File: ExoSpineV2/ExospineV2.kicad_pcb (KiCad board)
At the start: 2 copper layers, 79.5 x 73.1 mm, 54 parts, among them J1 JST PH 2pin, J11 2.54mm 4 pin header, J12 2.54mm 3 pin header, J13 JST PH 3pin, J14 JST PH 3pin, J15 JST PH 3pin, J16 JST PH 3pin, J17 JST PH 4pin, J18 JST PH 4pin, J19 2.54mm 4 pin header, J2 2.54mm 4 pin header, J20 2.54mm 3 pin header, J21 2.54mm 4 pin header, J22 2.54mm 3 pin header, J3 JST PH 3pin, J4 JST PH 3pin, J5 GPIO, J9 JST PH 2pin, Q4 2N7002, U1 MCP3008-I/SL, U2 74HC00, U3 74HC00

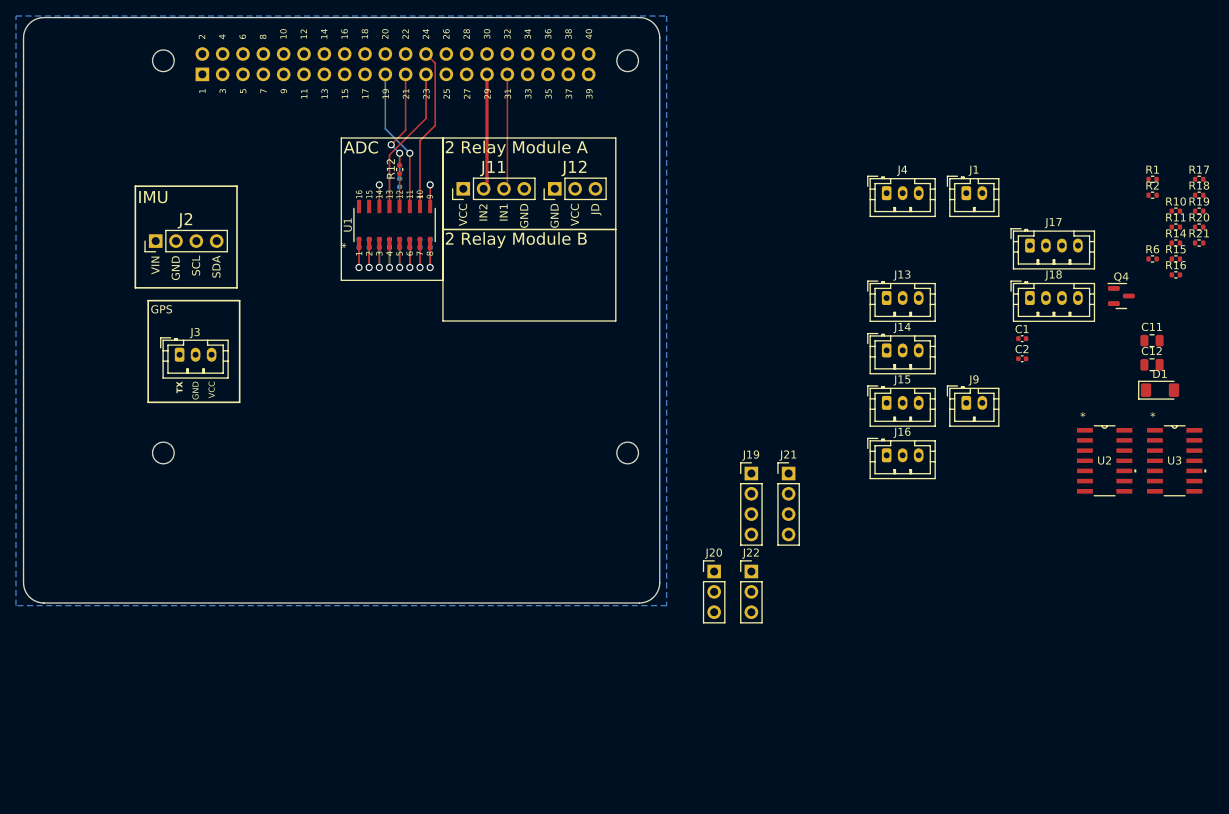
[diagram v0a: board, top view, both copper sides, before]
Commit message: positioned temperature sensors connectors on PCB
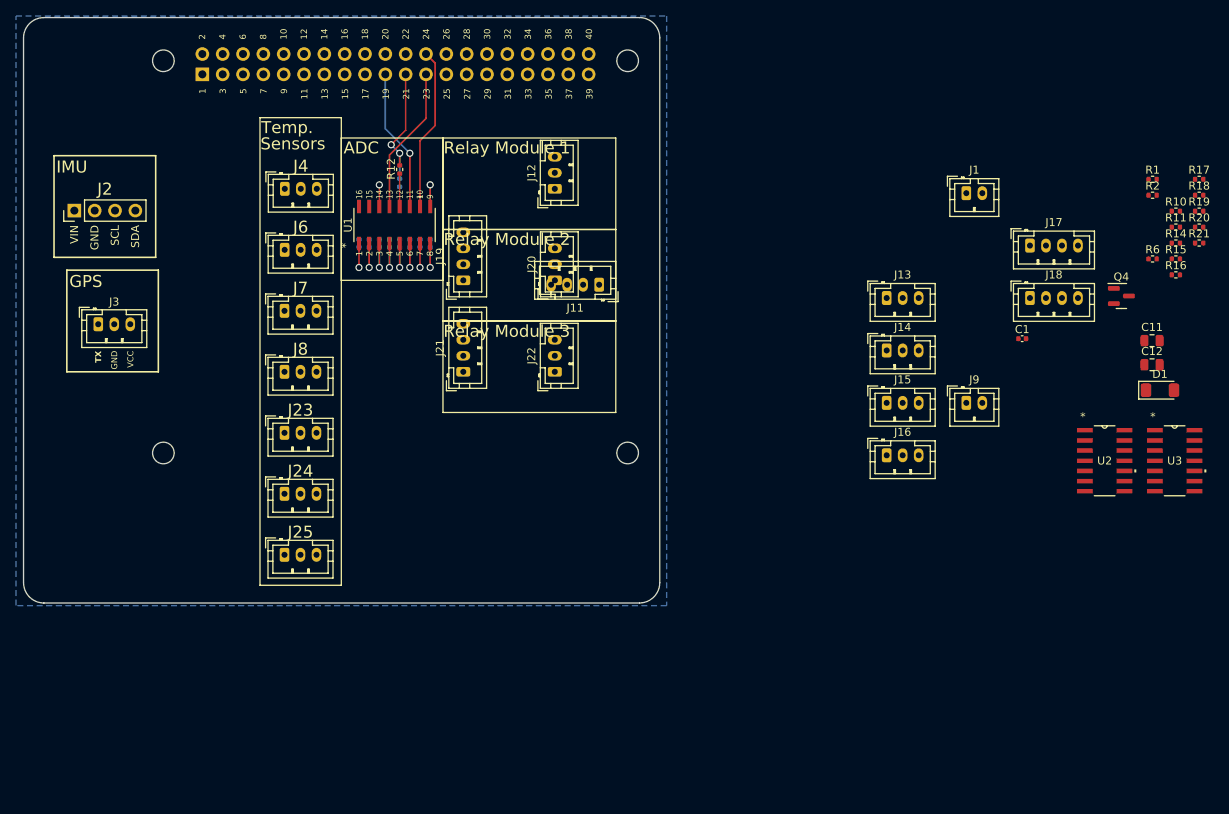
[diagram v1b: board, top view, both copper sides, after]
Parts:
- removed C2: 1uF, Capacitor_SMD:C_0402_1005Metric
- added J23: JST PH 3pin, Connector_JST:JST_PH_B3B-PH-K_1x03_P2.00mm_Vertical, F.Cu at (118.6, 94.0)
- added J24: JST PH 3pin, Connector_JST:JST_PH_B3B-PH-K_1x03_P2.00mm_Vertical, F.Cu at (118.6, 101.6)
- added J25: JST PH 3pin, Connector_JST:JST_PH_B3B-PH-K_1x03_P2.00mm_Vertical, F.Cu at (118.6, 109.2)
- added J6: JST PH 3pin, Connector_JST:JST_PH_B3B-PH-K_1x03_P2.00mm_Vertical, F.Cu at (118.7, 71.1)
- added J7: JST PH 3pin, Connector_JST:JST_PH_B3B-PH-K_1x03_P2.00mm_Vertical, F.Cu at (118.6, 78.7)
- added J8: JST PH 3pin, Connector_JST:JST_PH_B3B-PH-K_1x03_P2.00mm_Vertical, F.Cu at (118.6, 86.4)
- J11, J19, J21: value 2.54mm 4 pin header -> JST PH 4pin; footprint Connector_PinHeader_2.54mm:PinHeader_1x04_P2.54mm_Vertical -> Connector_JST:JST_PH_B4B-PH-K_1x04_P2.00mm_Vertical
- J12, J20, J22: value 2.54mm 3 pin header -> JST PH 3pin; footprint Connector_PinHeader_2.54mm:PinHeader_1x03_P2.54mm_Vertical -> Connector_JST:JST_PH_B3B-PH-K_1x03_P2.00mm_Vertical
- J2: value 2.54mm 4 pin header -> 2.54mm 4pin
- moved J4 75.2 mm to (118.7, 63.5)
- moved J19 43.3 mm to (141.0, 74.9), turned to 90 degrees
- moved J21 42.6 mm to (141.0, 86.4), turned to 90 degrees
- moved J20 41.5 mm to (152.4, 74.9), turned to 90 degrees
- moved J22 35.0 mm to (152.4, 86.4), turned to 90 degrees
- moved J11 20.8 mm to (157.9, 75.5), turned to 180 degrees
- moved J2 10.9 mm to (92.4, 66.2)
- moved J3 10.9 mm to (95.4, 80.4)
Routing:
- net /GPIO6: track 15.1 -> 0.00 mm
- net /GPIO5: track 15.1 -> 0.00 mm
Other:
- board text added: "Relay Module 1"
- board text added: "Relay Module 2"
- board text added: "Relay Module 3"
- board text added: "Sensors"
- board text added: "Temp."
- board text removed: "2 Relay Module A"
- board text removed: "2 Relay Module B"

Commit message: last commit before removing circuit for LTC4312 (I2C Multiplexer)
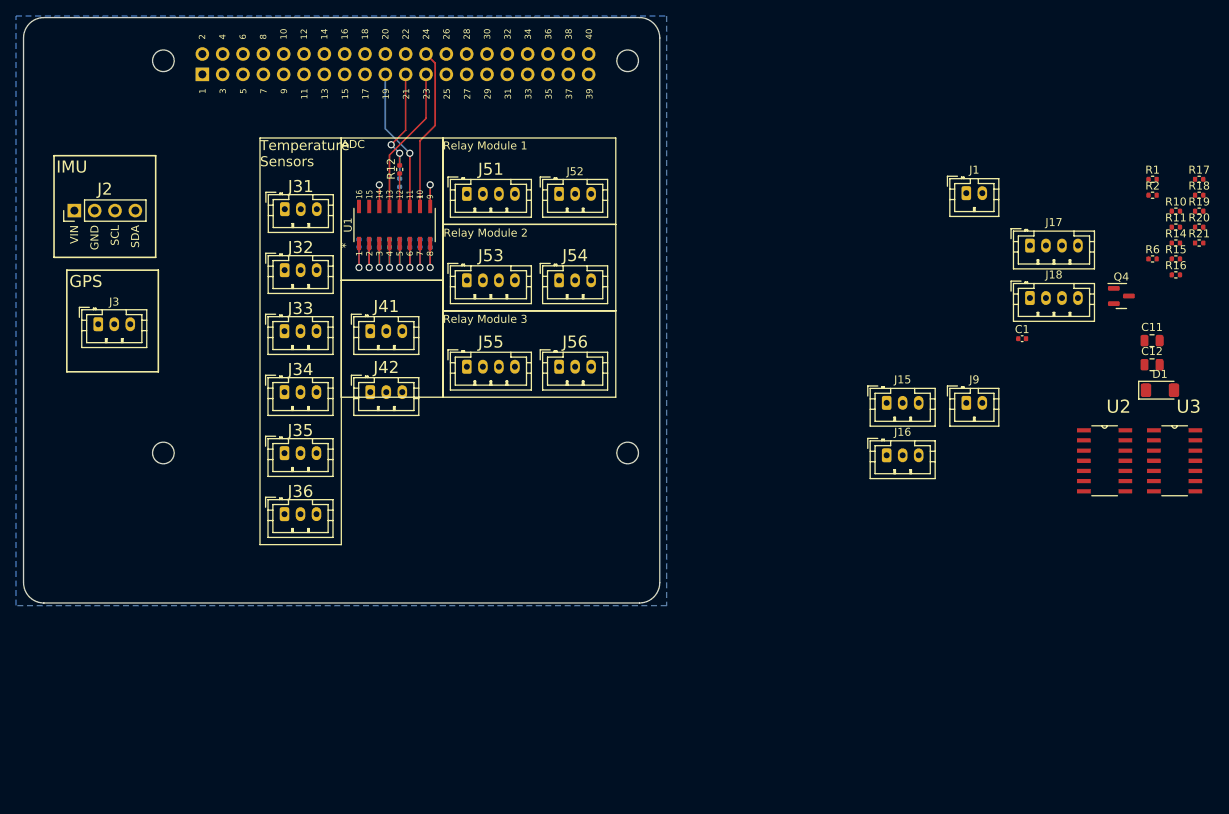
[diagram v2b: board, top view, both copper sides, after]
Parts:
- removed J25: JST PH 3pin, Connector_JST:JST_PH_B3B-PH-K_1x03_P2.00mm_Vertical
- U2, U3: value 74HC00 -> 74HC00D,653; footprint SNx4HC00:D14 -> ExoSpineV2:SOIC127P600X175-14N_74HC00D653
- moved J42 64.7 mm to (129.3, 88.9)
- moved J41 64.6 mm to (129.3, 81.3)
- moved J51 20.0 mm to (141.4, 64.1), turned to 0 degrees
- moved J31 2.54 mm to (118.7, 66.0)
- moved J33 2.54 mm to (118.6, 81.3)
- moved J34 2.54 mm to (118.6, 88.9)
- moved J36 2.54 mm to (118.6, 104.1)
- moved J32 2.54 mm to (118.7, 73.7)
- moved J35 2.54 mm to (118.6, 96.5)
- moved J52 0.83 mm to (152.9, 64.1), turned to 0 degrees
- moved J56 0.83 mm to (152.9, 85.7), turned to 0 degrees
- moved J55 0.78 mm to (141.4, 85.7), turned to 0 degrees
- moved J54 0.53 mm to (152.9, 74.9), turned to 0 degrees
- moved J53 0.44 mm to (141.4, 74.9), turned to 0 degrees
- renumbered J4 to J31, J6 to J32, J7 to J33, J8 to J34, J23 to J35, J24 to J36, J13 to J41, J14 to J42, J11 to J51, J12 to J52, J19 to J53, J20 to J54, J21 to J55, J22 to J56
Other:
- board text added: "Temperature Sensors"
- board text removed: "Sensors"
- board text removed: "Temp."

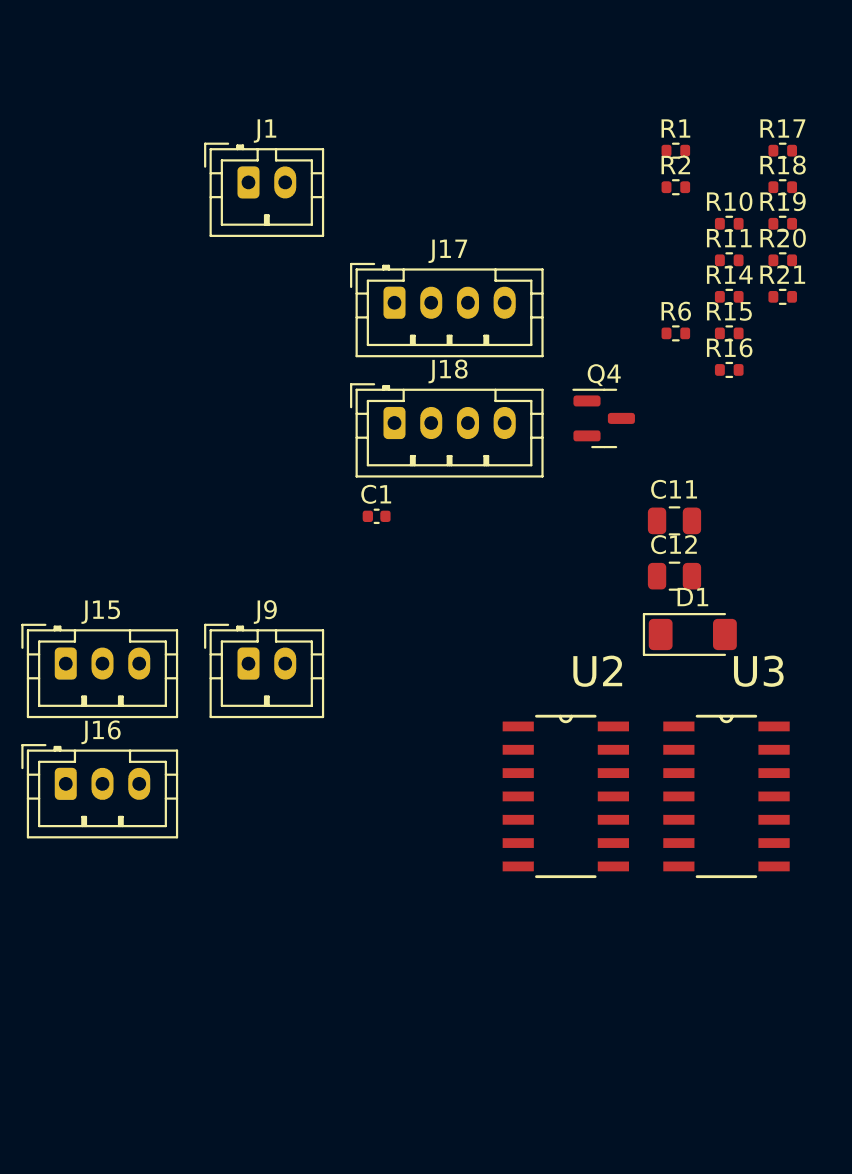
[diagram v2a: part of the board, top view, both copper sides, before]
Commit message: removed circuit for LTC4312 (I2C Multiplexer)
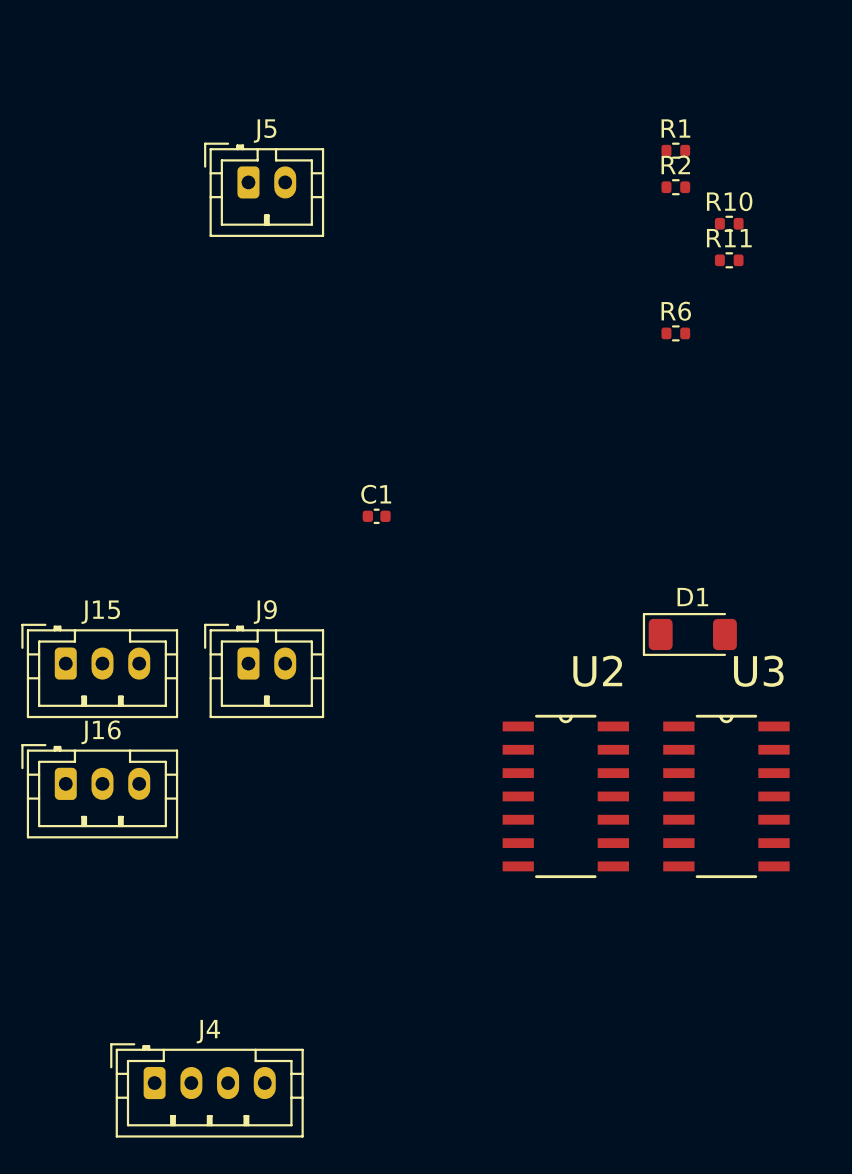
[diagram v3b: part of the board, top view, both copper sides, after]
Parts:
- removed C11, C12: 10nF, Capacitor_SMD:C_0805_2012Metric
- removed J17, J18: JST PH 4pin, Connector_JST:JST_PH_B4B-PH-K_1x04_P2.00mm_Vertical
- removed Q4: 2N7002, Package_TO_SOT_SMD:SOT-23
- removed R14, R15, R16, R17, R18, R19, R20, R21: 10k, Resistor_SMD:R_0402_1005Metric
- added J4: JST PH 4pin, Connector_JST:JST_PH_B4B-PH-K_1x04_P2.00mm_Vertical, F.Cu at (198.7, 113.1)
- renumbered J5 to J1, J1 to J5

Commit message: continued PCB
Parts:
- moved J55 3.81 mm to (141.4, 81.9)
- moved J56 3.81 mm to (152.9, 81.9)
- moved J53 2.54 mm to (141.4, 72.4)
- moved J54 2.54 mm to (152.9, 72.4)
- moved J33 1.91 mm to (118.7, 79.4)
- moved J35 1.91 mm to (118.7, 94.6)
- moved J36 1.91 mm to (118.7, 102.2)
- moved J31 1.91 mm to (118.7, 64.1)
- moved J32 1.91 mm to (118.7, 71.8)
- moved J34 1.82 mm to (118.7, 87.1)
- moved J51 1.27 mm to (141.4, 62.9)
- moved J52 1.27 mm to (152.9, 62.9)
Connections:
- J51 pad 2: /GPIO5 -> /GPIO12
- J51 pad 3: /GPIO6 -> /GPIO13
- J53 pad 2: /GPIO12 -> /GPIO16
- J53 pad 3: /GPIO13 -> unconnected-(J53-Pin_3-Pad3)
- J55 pad 2: /GPIO16 -> /GPIO5
- J55 pad 3: unconnected-(J55-Pin_3-Pad3) -> /GPIO6
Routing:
- net GND: track 5.42 -> 133.3 mm
- net +3.3V: track 0.00 -> 109.6 mm
- net +5V: track 0.00 -> 89.0 mm
- net /GPIO4/GPCLK0: track 0.00 -> 43.2 mm, vias 0 -> 1
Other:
- board text added: "Actuator Control"

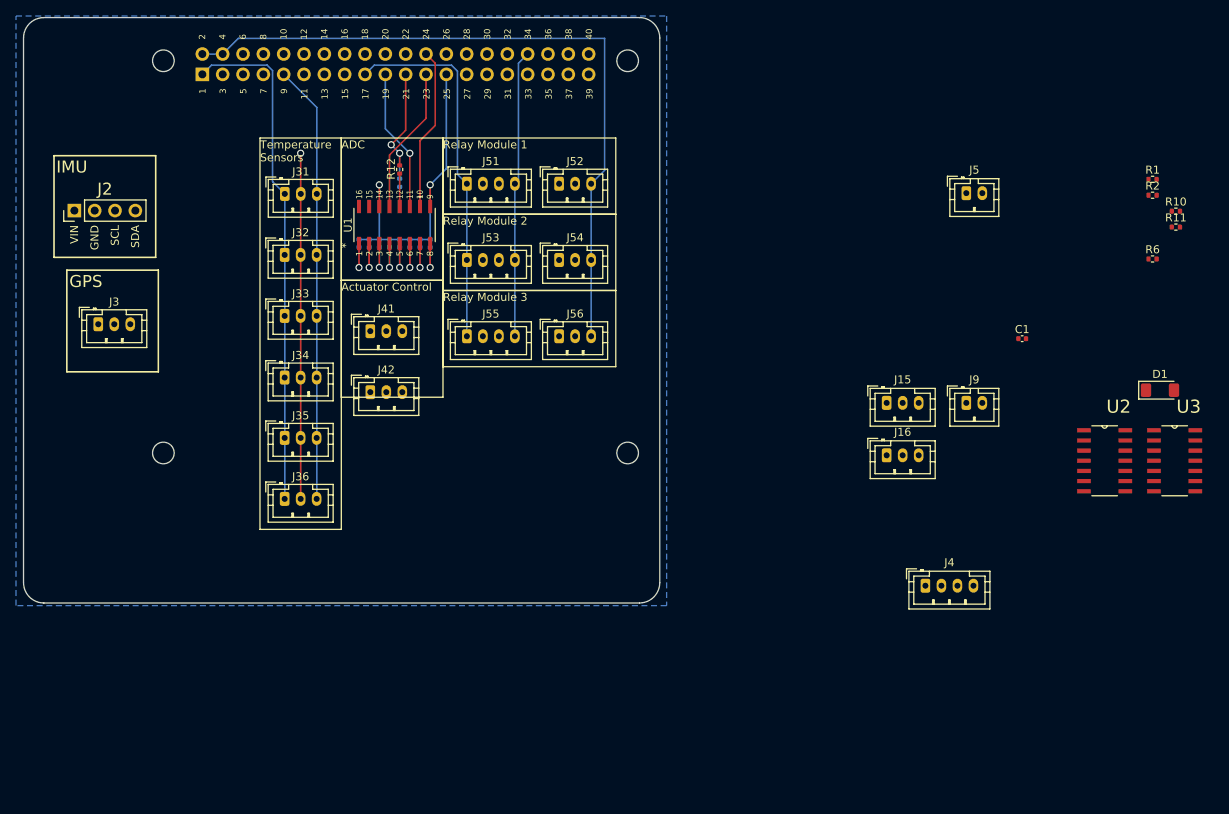
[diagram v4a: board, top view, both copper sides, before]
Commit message: changed actuator feedback circuit
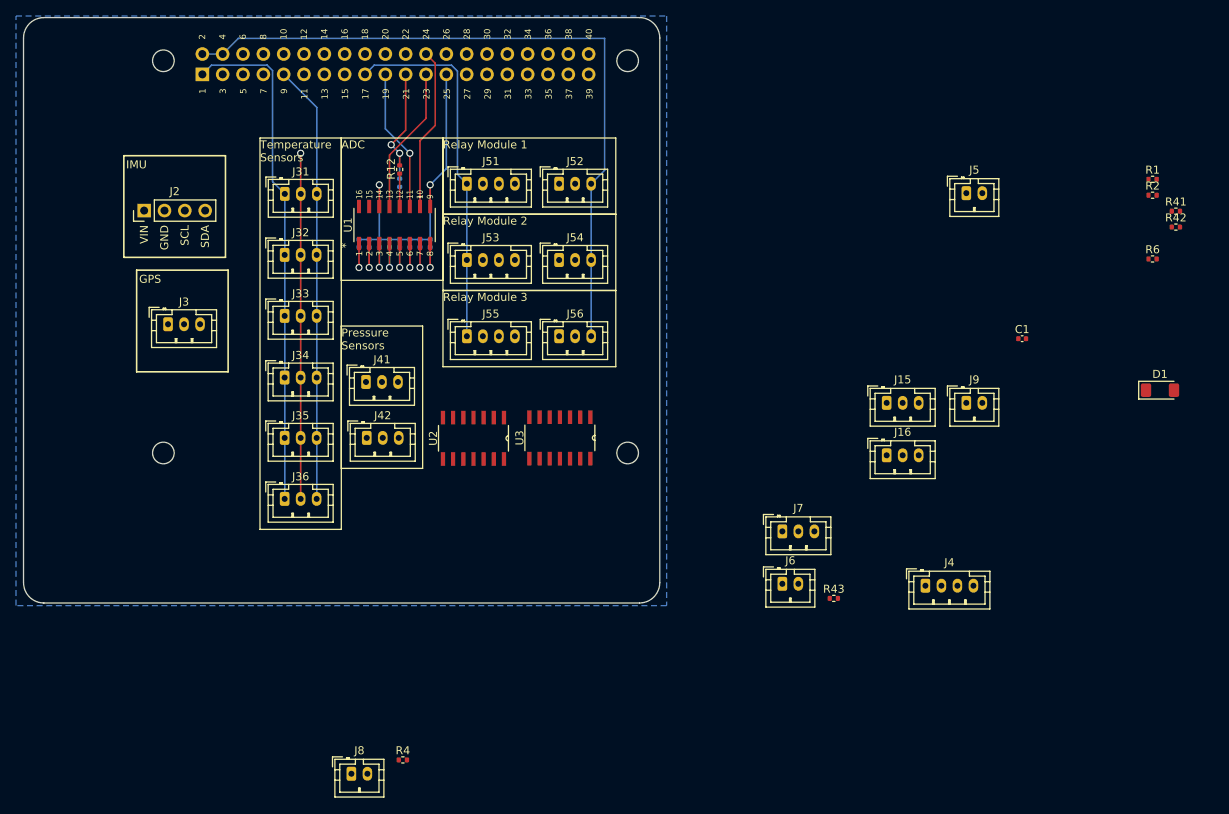
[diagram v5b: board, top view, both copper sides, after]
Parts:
- added J6: JST PH 2pin, Connector_JST:JST_PH_B2B-PH-K_1x02_P2.00mm_Vertical, F.Cu at (180.8, 112.8)
- added J7: JST PH 3pin, Connector_JST:JST_PH_B3B-PH-K_1x03_P2.00mm_Vertical, F.Cu at (180.8, 106.3)
- added J8: JST PH 2pin, Connector_JST:JST_PH_B2B-PH-K_1x02_P2.00mm_Vertical, F.Cu at (127.0, 136.6)
- added R4: 10k, Resistor_SMD:R_0402_1005Metric, F.Cu at (133.4, 134.8)
- added R43: 10k, Resistor_SMD:R_0402_1005Metric, F.Cu at (187.3, 114.7)
- moved U2 78.9 mm to (142.2, 94.7), turned to -90 degrees
- moved U3 76.9 mm to (153.0, 94.6), turned to -90 degrees
- moved J2 8.72 mm to (101.1, 66.2)
- moved J3 8.72 mm to (104.1, 80.4)
- moved J41 6.37 mm to (128.8, 87.6)
- moved J42 5.73 mm to (128.9, 94.6)
- renumbered R10 to R41, R11 to R42
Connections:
- J53 pad 2: /GPIO16 -> /DMS
- J53 pad 3: unconnected-(J53-Pin_3-Pad3) -> /GPIO16
- U2 pad 1: /GPIO23 -> Net-(J15-Pin_2)
- U2 pad 10: Net-(U2-Pad10) -> Net-(J15-Pin_3)
- U2 pad 12: Net-(U2-Pad12) -> Net-(U2-3Y)
- U2 pad 13: Net-(U2-Pad13) -> Net-(U2-1Y)
- U2 pad 3: Net-(U2-Pad10) -> Net-(U2-1Y)
- U2 pad 4: Net-(J15-Pin_2) -> /GPIO23
- U2 pad 6: Net-(U2-Pad12) -> Net-(U2-2Y)
- U2 pad 8: Net-(U2-Pad13) -> Net-(U2-3Y)
- U2 pad 9: Net-(J15-Pin_3) -> Net-(U2-2Y)
- U3 pad 1: /GPIO24 -> Net-(J16-Pin_2)
- U3 pad 10: Net-(U3-Pad10) -> Net-(J16-Pin_3)
- U3 pad 12: Net-(U3-Pad12) -> Net-(U3-3Y)
- U3 pad 13: Net-(U3-Pad13) -> Net-(U3-1Y)
- U3 pad 3: Net-(U3-Pad10) -> Net-(U3-1Y)
- U3 pad 4: Net-(J16-Pin_2) -> /GPIO24
- U3 pad 6: Net-(U3-Pad12) -> Net-(U3-2Y)
- U3 pad 8: Net-(U3-Pad13) -> Net-(U3-3Y)
- U3 pad 9: Net-(J16-Pin_3) -> Net-(U3-2Y)
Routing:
- net GND: track 133.3 -> 98.0 mm
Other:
- board text added: "Pressure Sensors"
- board text removed: "Actuator Control"
